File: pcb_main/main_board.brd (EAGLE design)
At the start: 82 x 81.2 mm, 66 parts, among them IC7 LM1117IMPX-5.0, Q1 FDS5680, T1 BC847, U1 STM32F411RET6, X1 FH12-14S-0.5SH

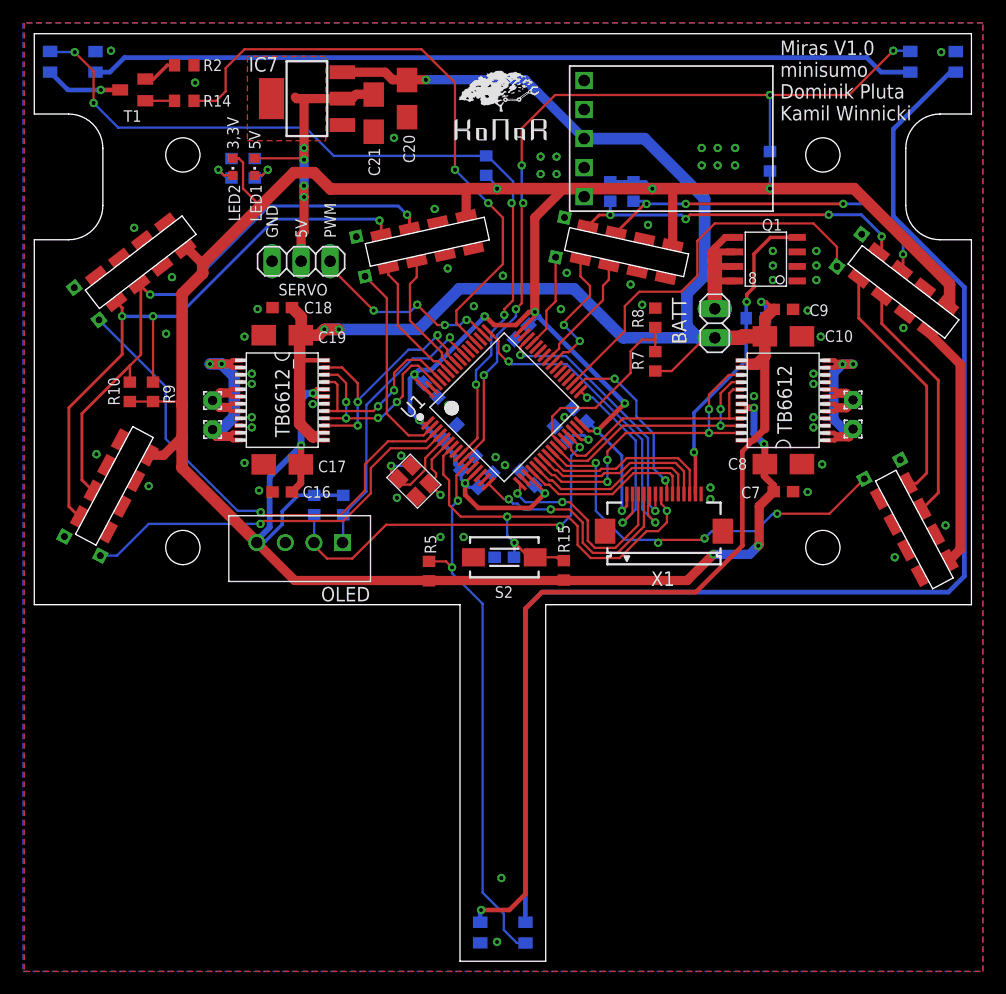
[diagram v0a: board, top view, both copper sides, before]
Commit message: improved routing
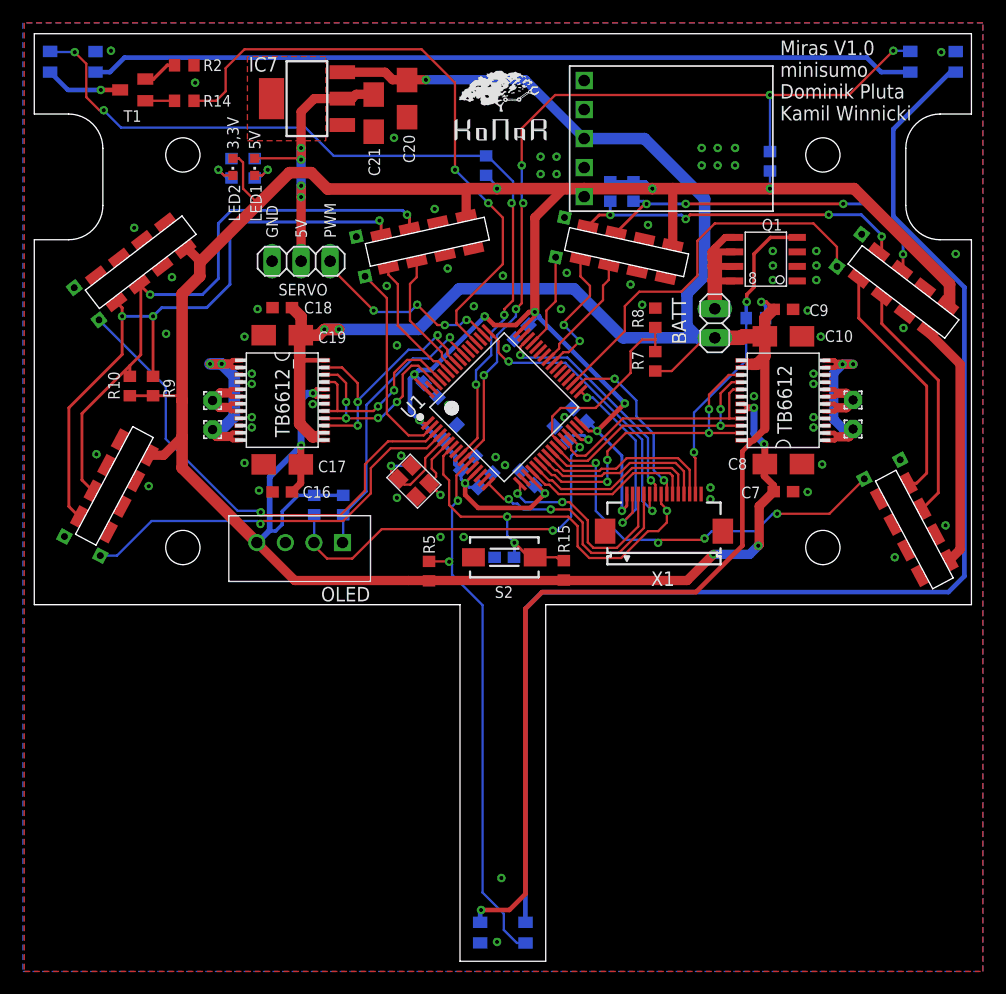
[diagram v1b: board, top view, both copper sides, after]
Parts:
- moved R10 0.51 mm to (-32.6, 14.2)
- moved R9 0.51 mm to (-30.6, 14.2)
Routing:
- net SWDIO: track 24.0 -> 21.0 mm
- net SWCLK: track 28.5 -> 26.2 mm
- net SDA_1: track 65.9 -> 68.1 mm
- net SCL_1: track 61.8 -> 63.8 mm
- net 5V: track 27.8 -> 26.2 mm
- net ROBOT_OFF: track 28.1 -> 27.6 mm
- net 3,3V: track 339.6 -> 339.1 mm
- net GND: vias 68 -> 71

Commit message: corrected on
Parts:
- added R18: 1k, rcl:R0603
- Q1: value FDS5680 -> (none); device transistor-fet:SO-8 -> transistor-power:SO-08
- moved Q1 9.84 mm to (16.1, 18.3)
- moved BATT 7.00 mm to (23.5, 24.6), turned to 180 degrees
- moved R8 1.80 mm to (12.1, 18.9)
- moved R1 1.67 mm to (20.5, 20.2), turned to 90 degrees
- moved R7 1.48 mm to (12.1, 15.6)
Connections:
- removed net BAT-: BATT.1, Q1.5, Q1.6, Q1.7, Q1.8
- new net BAT: BATT.2, Q1.1, Q1.2, Q1.3, R1.2
- new net N$8: Q1.4, R1.1, R18.2
- net BAT+: now also Q1.5, Q1.6, Q1.7, Q1.8; no longer BATT.2, R1.2
- net GND: now also BATT.1; no longer Q1.1, Q1.2, Q1.3
- net ROBOT_OFF: now also R18.1; no longer Q1.4, R1.1
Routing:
- net ROBOT_OFF: track 27.6 -> 2.17 mm, vias 2 -> 0
- net BAT: track 0.00 -> 21.8 mm
- net N$8: track 0.00 -> 21.4 mm, vias 0 -> 2
- net BAT-: track 14.0 -> 0.00 mm
- net BAT+: track 201.4 -> 205.2 mm, vias 5 -> 6
- net BAT_MEAS: track 17.7 -> 14.7 mm
- net 3,3V: track 339.1 -> 340.0 mm
- net GND: vias 71 -> 66

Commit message: adjust component values
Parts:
- C1, C2: value 22p -> 18p
- R16: value 1k? -> 10k
- R17: value 470R? -> 3k3
- R2: value 130R -> 100R
- R7: value 33k? -> 10k
- R8: value 10k -> 3k3
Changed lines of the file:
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@@
 <drawing>
 <settings>
-<setting alwaysvectorfont="yes"/>
+<setting alwaysvectorfont="no"/>
 <setting verticaltext="up"/>
 </settings>
@@
 <attribute name="VALUE" x="10.3494" y="1.1982" size="1.27" layer="27"/>
 </element>
-<element name="R7" library="rcl" library_urn="urn:adsk.eagle:library:334" package="R0603" package3d_urn="urn:adsk.eagle:package:23555/3" value="33k?" x="12.065" y="15.621" smashed="yes" rot="R90">
+<element name="R7" library="rcl" library_urn="urn:adsk.eagle:library:334" package="R0603" package3d_urn="urn:adsk.eagle:package:23555/3" value="10k" x="12.065" y="15.621" smashed="yes" rot="R90">
 <attribute name="NAME" x="11.049" y="14.859" size="1.016" layer="25" rot="R90"/>
 <attribute name="POPULARITY" value="70" x="12.065" y="15.621" size="1.778" layer="27" rot="R90" display="off"/>
@@
 <attribute name="VALUE" x="13.97" y="14.986" size="1.27" layer="27" rot="R90"/>
 </element>
-<element name="R8" library="rcl" library_urn="urn:adsk.eagle:library:334" package="R0603" package3d_urn="urn:adsk.eagle:package:23555/3" value="10k" x="12.065" y="18.923" smashed="yes" rot="R90">
+<element name="R8" library="rcl" library_urn="urn:adsk.eagle:library:334" package="R0603" package3d_urn="urn:adsk.eagle:package:23555/3" value="3k3" x="12.065" y="18.923" smashed="yes" rot="R90">
 <attribute name="NAME" x="11.049" y="18.034" size="1.016" layer="25" rot="R90"/>
 <attribute name="POPULARITY" value="70" x="12.065" y="18.923" size="1.778" layer="27" rot="R90" display="off"/>
@@
 </element>
 <element name="U$8" library="CRYSTAL_SMD_3,4x2.7mm" package="CRYSTAL_3,4X2,7" override_package3d_urn="urn:adsk.eagle:package:39279074/2" override_package_urn="urn:adsk.eagle:footprint:39279075/1" value="8MHz" x="-8.001" y="7.239" smashed="yes" rot="R315"/>
-<element name="C1" library="rcl" library_urn="urn:adsk.eagle:library:334" package="C0603" package3d_urn="urn:adsk.eagle:package:23616/2" value="22p" x="-6.985" y="5.08" smashed="yes" rot="MR315">
+<element name="C1" library="rcl" library_urn="urn:adsk.eagle:library:334" package="C0603" package3d_urn="urn:adsk.eagle:package:23616/2" value="18p" x="-6.985" y="5.08" smashed="yes" rot="MR315">
 <attribute name="NAME" x="-7.874" y="3.565025" size="1.016" layer="26" rot="MR315"/>
 <attribute name="POPULARITY" value="73" x="-6.985" y="5.08" size="1.778" layer="28" rot="MR315" display="off"/>
@@
 <attribute name="VALUE" x="-5.188946875" y="4.181971875" size="1.27" layer="28" rot="MR315"/>
 </element>
-<element name="C2" library="rcl" library_urn="urn:adsk.eagle:library:334" package="C0603" package3d_urn="urn:adsk.eagle:package:23616/2" value="22p" x="-8.509" y="6.604" smashed="yes" rot="MR315">
+<element name="C2" library="rcl" library_urn="urn:adsk.eagle:library:334" package="C0603" package3d_urn="urn:adsk.eagle:package:23616/2" value="18p" x="-8.509" y="6.604" smashed="yes" rot="MR315">
 <attribute name="NAME" x="-9.398" y="5.089025" size="1.016" layer="26" rot="MR315"/>
 <attribute name="POPULARITY" value="73" x="-8.509" y="6.604" size="1.778" layer="28" rot="MR315" display="off"/>
@@
 <attribute name="VALUE" x="-29.21" y="38.227" size="1.27" layer="27" rot="R90"/>
 </element>
-<element name="R2" library="rcl" library_urn="urn:adsk.eagle:library:334" package="R0603" package3d_urn="urn:adsk.eagle:package:23555/3" value="130R" x="-27.8765" y="42.291" smashed="yes">
+<element name="R2" library="rcl" library_urn="urn:adsk.eagle:library:334" package="R0603" package3d_urn="urn:adsk.eagle:package:23555/3" value="100R" x="-27.8765" y="42.291" smashed="yes">
 <attribute name="NAME" x="-26.2255" y="41.783" size="1.016" layer="25"/>
 <attribute name="POPULARITY" value="70" x="-27.8765" y="42.291" size="1.778" layer="27" display="off"/>
@@
 <attribute name="VALUE" x="-20.717" y="35.401" size="1.27" layer="27" rot="R180"/>
 </element>
-<element name="R16" library="rcl" library_urn="urn:adsk.eagle:library:334" package="R0603" package3d_urn="urn:adsk.eagle:package:23555/3" value="1k?" x="-21.717" y="33.274" smashed="yes" rot="MR90">
+<element name="R16" library="rcl" library_urn="urn:adsk.eagle:library:334" package="R0603" package3d_urn="urn:adsk.eagle:package:23555/3" value="10k" x="-21.717" y="33.274" smashed="yes" rot="MR90">
 <attribute name="NAME" x="-22.225" y="34.925" size="1.016" layer="26" rot="MR90"/>
 <attribute name="POPULARITY" value="70" x="-21.717" y="33.274" size="0.02031875" layer="28" font="vector" rot="MR90" display="off"/>
@@
 <attribute name="VALUE" x="-25.527" y="34.671" size="1.27" layer="27" rot="R270"/>
 </element>
-<element name="R17" library="rcl" library_urn="urn:adsk.eagle:library:334" package="R0603" package3d_urn="urn:adsk.eagle:package:23555/3" value="470R?" x="-23.749" y="33.274" smashed="yes" rot="MR90">
+<element name="R17" library="rcl" library_urn="urn:adsk.eagle:library:334" package="R0603" package3d_urn="urn:adsk.eagle:package:23555/3" value="3k3" x="-23.749" y="33.274" smashed="yes" rot="MR90">
 <attribute name="NAME" x="-24.257" y="34.925" size="1.016" layer="26" rot="MR90"/>
 <attribute name="POPULARITY" value="70" x="-18.796" y="28.321" size="1.016" layer="28" font="vector" rot="MR90" display="off"/>
